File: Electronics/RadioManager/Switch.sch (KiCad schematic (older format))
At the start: 2 parts

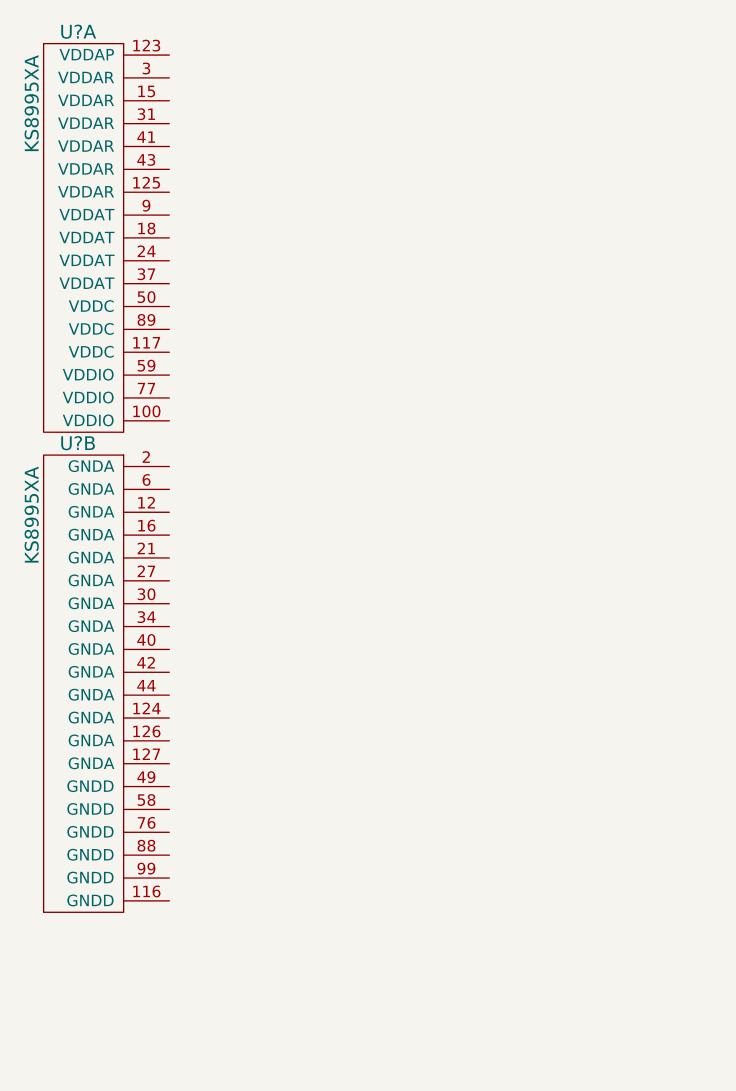
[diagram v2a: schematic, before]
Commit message: Replace switch with industrial version
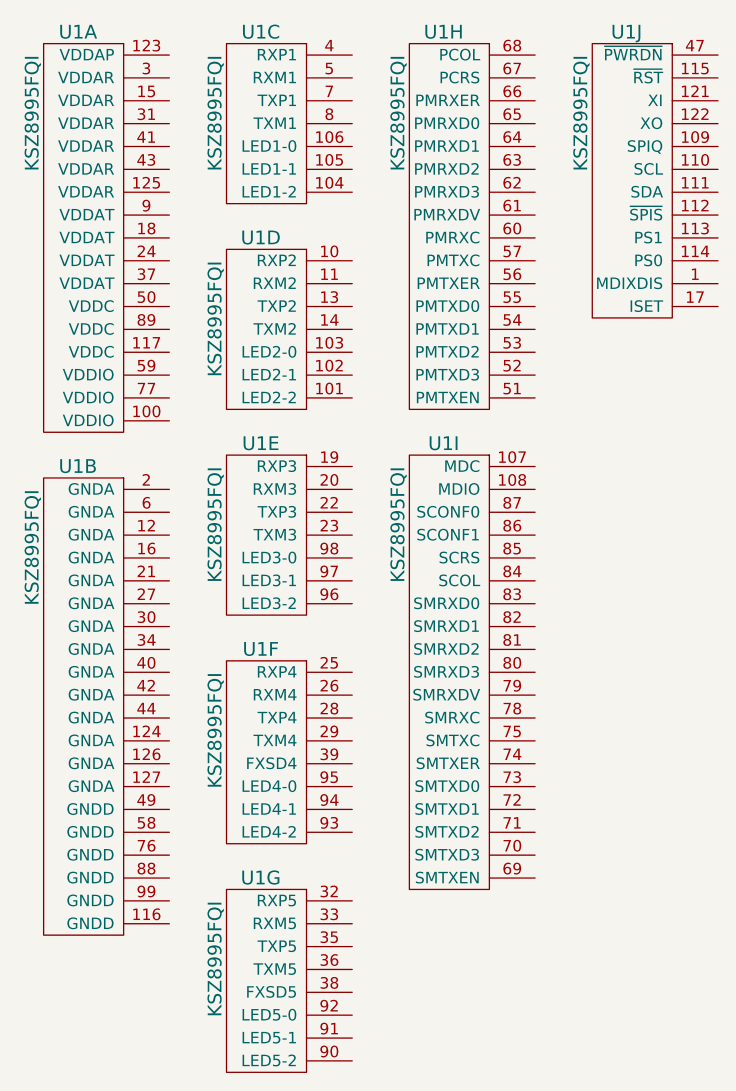
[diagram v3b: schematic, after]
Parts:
- removed U?: KS8995XA, ~, symbol KS8995XA
- added unit 2 of U1
- added unit 3 of U1
- added unit 4 of U1
- added unit 5 of U1
- added unit 6 of U1
- added unit 7 of U1
- added unit 8 of U1
- added unit 9 of U1
- added unit 10 of U1
- U1: renamed from U?; value KS8995XA -> KSZ8995FQI; Distributor Part No (none) -> 576-3300-ND; MFR Name (none) -> Micrel; MFR Part No (none) -> KSZ8995FQI
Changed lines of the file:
@@
 $EndDescr
 $Comp
-L KS8995XA U?
+L KS8995XA U1
 U 1 1 53DFFDCD
 P 1800 1700
-F 0 "U?" H 1800 1800 60  0000 C CNN
-F 1 "KS8995XA" V 1600 1700 60  0000 R CNN
+F 0 "U1" H 1800 1800 60  0000 C CNN
+F 1 "KSZ8995FQI" V 1600 1700 60  0000 R CNN
 F 2 "~" H 1800 1700 60  0000 C CNN
 F 3 "~" H 1800 1700 60  0000 C CNN
+F 4 "Micrel" H 1800 1700 60  0001 C CNN "MFR Name"
+F 5 "KSZ8995FQI" H 1800 1700 60  0001 C CNN "MFR Part No"
+F 6 "576-3300-ND" H 1800 1700 60  0001 C CNN "Distributor Part No"
 	1    1800 1700
 	1    0    0    -1
 $EndComp
 $Comp
-L KS8995XA U?
-U 2 1 53DFFDDC
-P 1800 3500
-F 0 "U?" H 1800 3600 60  0000 C CNN
-F 1 "KS8995XA" V 1600 3500 60  0000 R CNN
-F 2 "~" H 1800 3500 60  0000 C CNN
-F 3 "~" H 1800 3500 60  0000 C CNN
-	2    1800 3500
+L KS8995XA U1
+U 2 1 5410EF74
+P 1800 3600
+F 0 "U1" H 1800 3700 60  0000 C CNN
+F 1 "KSZ8995FQI" V 1600 3600 60  0000 R CNN
+F 2 "~" H 1800 3600 60  0000 C CNN
+F 3 "~" H 1800 3600 60  0000 C CNN
+F 4 "Micrel" H 1800 3600 60  0001 C CNN "MFR Name"
+F 5 "KSZ8995FQI" H 1800 3600 60  0001 C CNN "MFR Part No"
+F 6 "576-3300-ND" H 1800 3600 60  0001 C CNN "Distributor Part No"
+	2    1800 3600
 	1    0    0    -1
 $EndComp
+$Comp
+L KS8995XA U1
+U 3 1 5410EF88
+P 2600 1700
+F 0 "U1" H 2600 1800 60  0000 C CNN
+F 1 "KSZ8995FQI" V 2400 1700 60  0000 R CNN
+F 2 "~" H 2600 1700 60  0000 C CNN
+F 3 "~" H 2600 1700 60  0000 C CNN
+F 4 "Micrel" H 2600 1700 60  0001 C CNN "MFR Name"
+F 5 "KSZ8995FQI" H 2600 1700 60  0001 C CNN "MFR Part No"
+F 6 "576-3300-ND" H 2600 1700 60  0001 C CNN "Distributor Part No"
+	3    2600 1700
+	1    0    0    -1
+$EndComp
+$Comp
+L KS8995XA U1
+U 4 1 5410EF99
+P 2600 2600
+F 0 "U1" H 2600 2700 60  0000 C CNN
+F 1 "KSZ8995FQI" V 2400 2600 60  0000 R CNN
+F 2 "~" H 2600 2600 60  0000 C CNN
+F 3 "~" H 2600 2600 60  0000 C CNN
+F 4 "Micrel" H 2600 2600 60  0001 C CNN "MFR Name"
+F 5 "KSZ8995FQI" H 2600 2600 60  0001 C CNN "MFR Part No"
+F 6 "576-3300-ND" H 2600 2600 60  0001 C CNN "Distributor Part No"
+	4    2600 2600
+	1    0    0    -1
+$EndComp
+$Comp
+L KS8995XA U1
+U 5 1 5410EFAA
+P 2600 3500
+F 0 "U1" H 2600 3600 60  0000 C CNN
+F 1 "KSZ8995FQI" V 2400 3500 60  0000 R CNN
+F 2 "~" H 2600 3500 60  0000 C CNN
+F 3 "~" H 2600 3500 60  0000 C CNN
+F 4 "Micrel" H 2600 3500 60  0001 C CNN "MFR Name"
+F 5 "KSZ8995FQI" H 2600 3500 60  0001 C CNN "MFR Part No"
+F 6 "576-3300-ND" H 2600 3500 60  0001 C CNN "Distributor Part No"
+	5    2600 3500
+	1    0    0    -1
+$EndComp
+$Comp
+L KS8995XA U1
+U 6 1 5410EFBB
+P 2600 4400
+F 0 "U1" H 2600 4500 60  0000 C CNN
+F 1 "KSZ8995FQI" V 2400 4400 60  0000 R CNN
+F 2 "~" H 2600 4400 60  0000 C CNN
+F 3 "~" H 2600 4400 60  0000 C CNN
+F 4 "Micrel" H 2600 4400 60  0001 C CNN "MFR Name"
+F 5 "KSZ8995FQI" H 2600 4400 60  0001 C CNN "MFR Part No"
+F 6 "576-3300-ND" H 2600 4400 60  0001 C CNN "Distributor Part No"
+	6    2600 4400
+	1    0    0    -1
+$EndComp
+$Comp
+L KS8995XA U1
+U 7 1 5410EFCC
+P 2600 5400
+F 0 "U1" H 2600 5500 60  0000 C CNN
+F 1 "KSZ8995FQI" V 2400 5400 60  0000 R CNN
+F 2 "~" H 2600 5400 60  0000 C CNN
+F 3 "~" H 2600 5400 60  0000 C CNN
+F 4 "Micrel" H 2600 5400 60  0001 C CNN "MFR Name"
+F 5 "KSZ8995FQI" H 2600 5400 60  0001 C CNN "MFR Part No"
+F 6 "576-3300-ND" H 2600 5400 60  0001 C CNN "Distributor Part No"
+	7    2600 5400
+	1    0    0    -1
+$EndComp
+$Comp
+L KS8995XA U1
+U 8 1 5410EFDD
+P 3400 1700
+F 0 "U1" H 3400 1800 60  0000 C CNN
+F 1 "KSZ8995FQI" V 3200 1700 60  0000 R CNN
+F 2 "~" H 3400 1700 60  0000 C CNN
+F 3 "~" H 3400 1700 60  0000 C CNN
+F 4 "Micrel" H 3400 1700 60  0001 C CNN "MFR Name"
+F 5 "KSZ8995FQI" H 3400 1700 60  0001 C CNN "MFR Part No"
+F 6 "576-3300-ND" H 3400 1700 60  0001 C CNN "Distributor Part No"
+	8    3400 1700
+	1    0    0    -1
+$EndComp
+$Comp
+L KS8995XA U1
+U 9 1 5410EFEE
+P 3400 3500
+F 0 "U1" H 3400 3600 60  0000 C CNN
+F 1 "KSZ8995FQI" V 3200 3500 60  0000 R CNN
+F 2 "~" H 3400 3500 60  0000 C CNN
+F 3 "~" H 3400 3500 60  0000 C CNN
+F 4 "Micrel" H 3400 3500 60  0001 C CNN "MFR Name"
+F 5 "KSZ8995FQI" H 3400 3500 60  0001 C CNN "MFR Part No"
+F 6 "576-3300-ND" H 3400 3500 60  0001 C CNN "Distributor Part No"
+	9    3400 3500
+	1    0    0    -1
+$EndComp
+$Comp
+L KS8995XA U1
+U 10 1 5410EFFF
+P 4200 1700
+F 0 "U1" H 4200 1800 60  0000 C CNN
+F 1 "KSZ8995FQI" V 4000 1700 60  0000 R CNN
+F 2 "~" H 4200 1700 60  0000 C CNN
+F 3 "~" H 4200 1700 60  0000 C CNN
+F 4 "Micrel" H 4200 1700 60  0001 C CNN "MFR Name"
+F 5 "KSZ8995FQI" H 4200 1700 60  0001 C CNN "MFR Part No"
+F 6 "576-3300-ND" H 4200 1700 60  0001 C CNN "Distributor Part No"
+	10   4200 1700
+	1    0    0    -1
+$EndComp

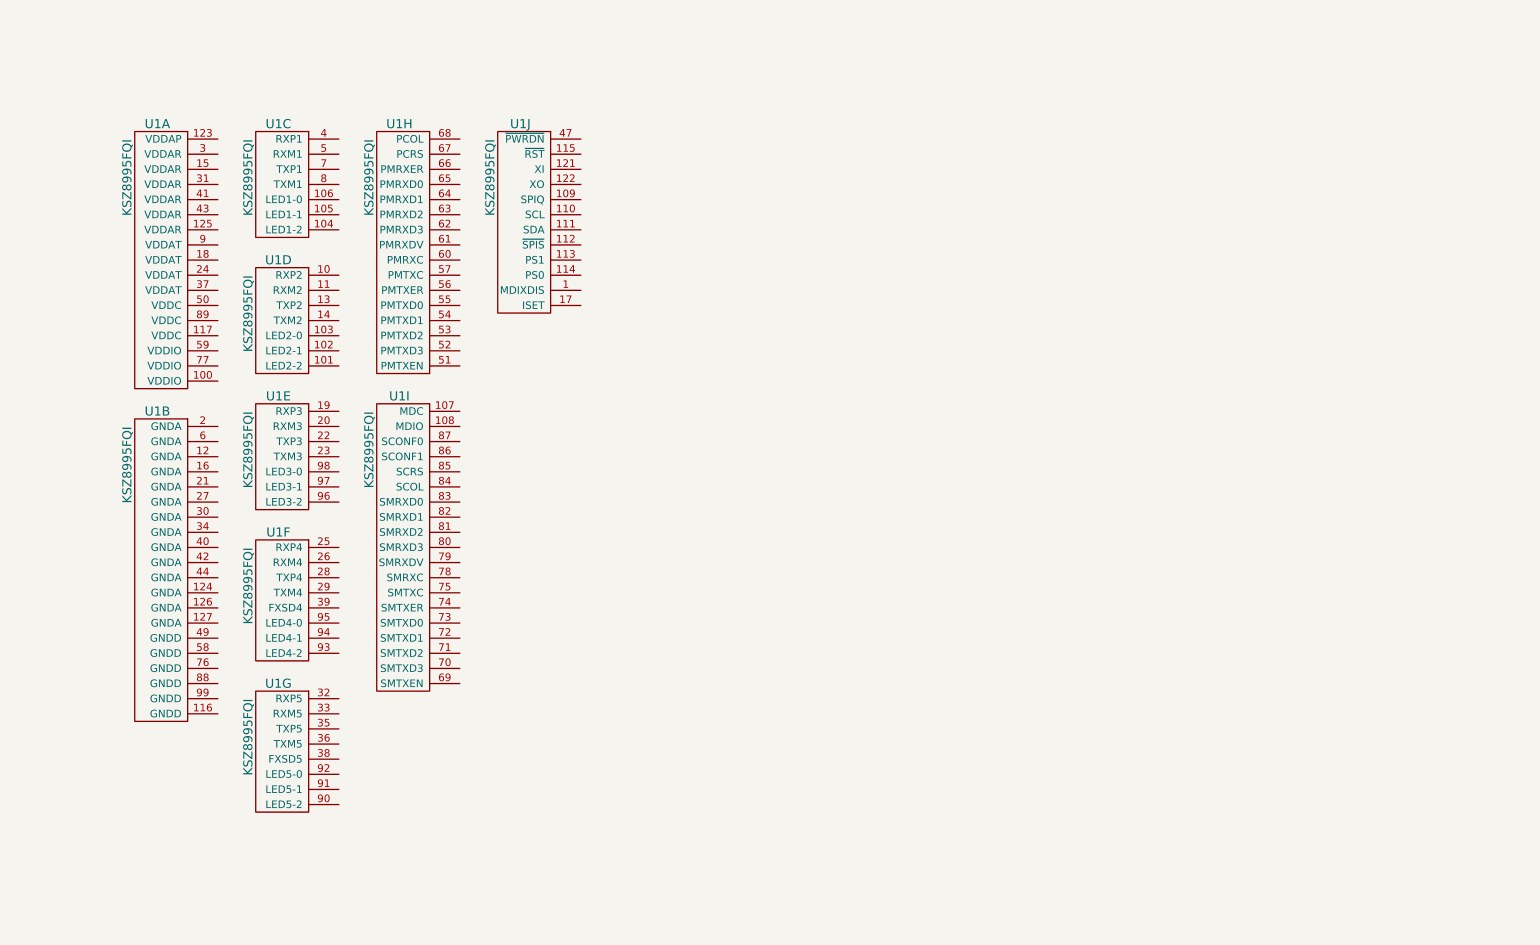
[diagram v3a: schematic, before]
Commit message: Switch power connections
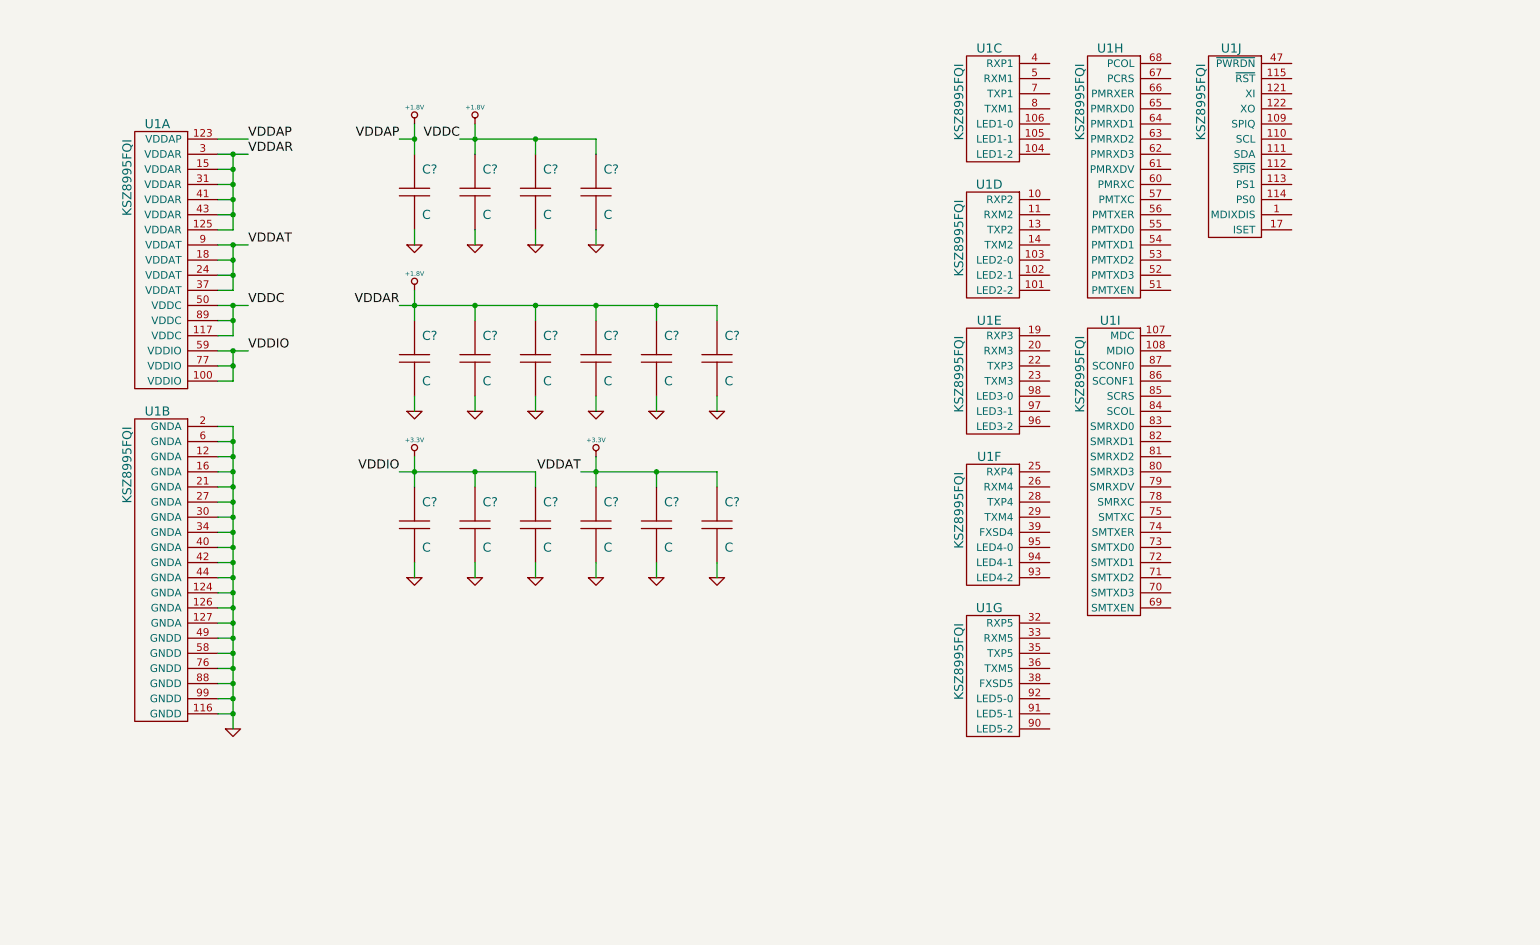
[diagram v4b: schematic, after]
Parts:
- added C? (x16): C, ~, symbol C
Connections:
- net +3.3V: now reaches U1.100 (VDDIO)
- net +3.3V: now also U1.18 (VDDAT), U1.24 (VDDAT), U1.37 (VDDAT), U1.59 (VDDIO), U1.77 (VDDIO), U1.9 (VDDAT), C?.1, C?.1, C?.1, C?.1, C?.1, C?.1
- net +1.8V: now reaches U1.117 (VDDC)
- net +1.8V: now also U1.123 (VDDAP), U1.125 (VDDAR), U1.15 (VDDAR), U1.3 (VDDAR), U1.31 (VDDAR), U1.41 (VDDAR), U1.43 (VDDAR), U1.50 (VDDC), U1.89 (VDDC), C?.1, C?.1, C?.1, C?.1, C?.1, C?.1, C?.1, C?.1, C?.1, C?.1
- net GND: now reaches U1.116 (GNDD)
- net GND: now also U1.12 (GNDA), U1.124 (GNDA), U1.126 (GNDA), U1.127 (GNDA), U1.16 (GNDA), U1.2 (GNDA), U1.21 (GNDA), U1.27 (GNDA), U1.30 (GNDA), U1.34 (GNDA), U1.40 (GNDA), U1.42 (GNDA), U1.44 (GNDA), U1.49 (GNDD), U1.58 (GNDD), U1.6 (GNDA), U1.76 (GNDD), U1.88 (GNDD), U1.99 (GNDD), C?.2, C?.2, C?.2, C?.2, C?.2, C?.2, C?.2, C?.2, C?.2, C?.2, C?.2, C?.2, C?.2, C?.2, C?.2, C?.2
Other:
- moved on the sheet: U1C, U1D, U1E, U1F, U1G, U1H, U1I, U1J

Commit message: Add port connections
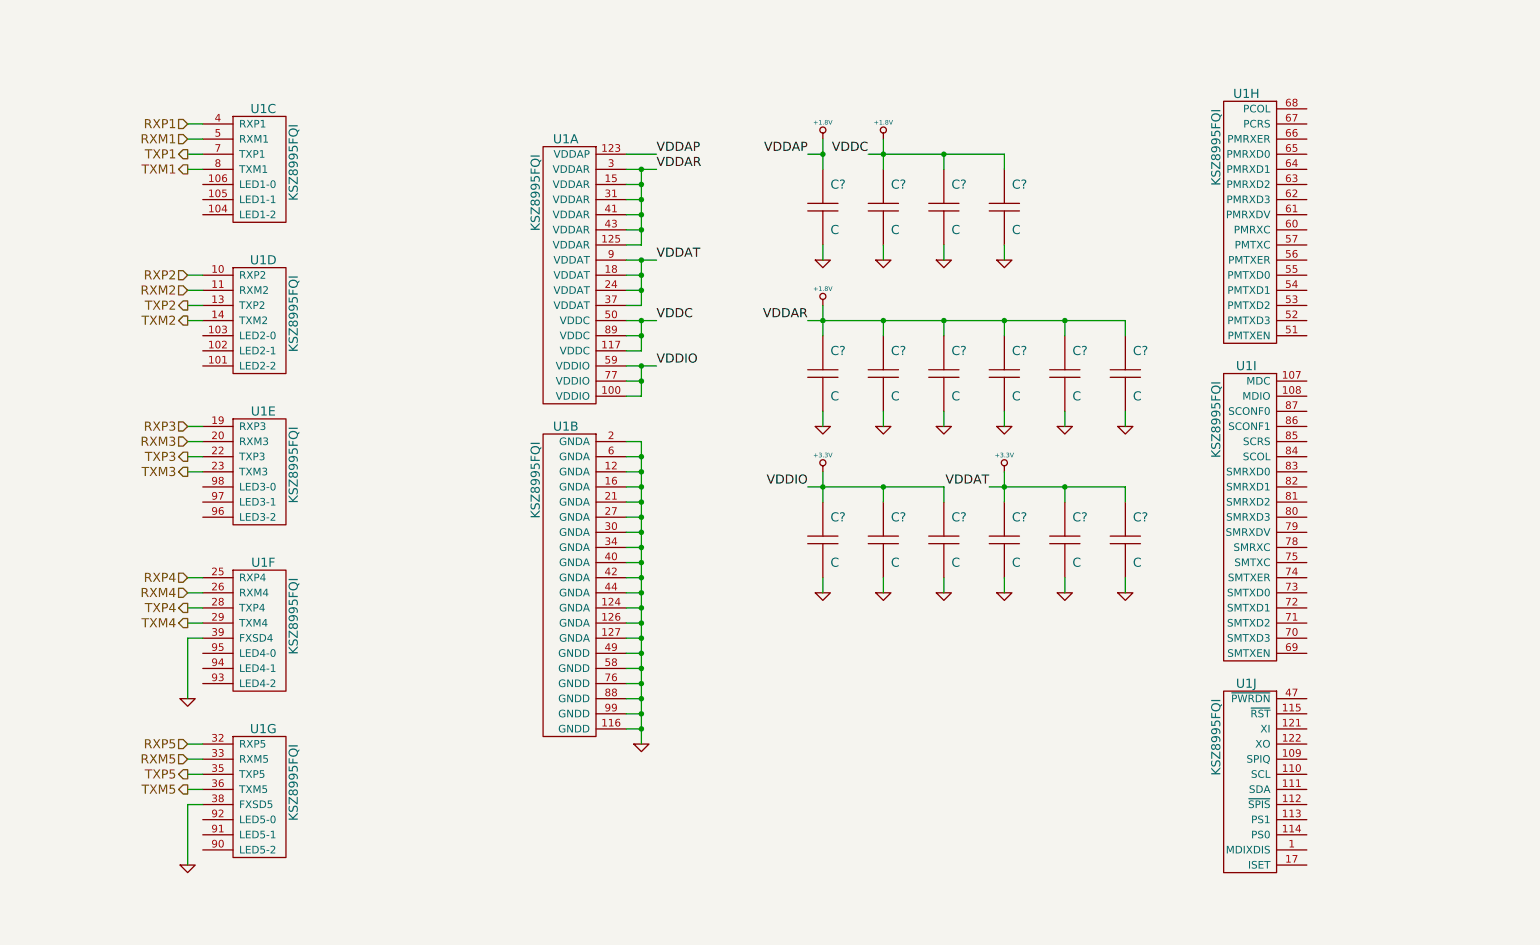
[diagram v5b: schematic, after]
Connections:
- net GND: now also U1.38 (FXSD5), U1.39 (FXSD4)
- net RXP1: now reaches U1.4 (RXP1)
- net RXM1: now reaches U1.5 (RXM1)
- net TXP1: now reaches U1.7 (TXP1)
- net TXM1: now reaches U1.8 (TXM1)
- net RXP2: now reaches U1.10 (RXP2)
- net RXM2: now reaches U1.11 (RXM2)
- net TXP2: now reaches U1.13 (TXP2)
- net TXM2: now reaches U1.14 (TXM2)
- net RXP3: now reaches U1.19 (RXP3)
- net RXM3: now reaches U1.20 (RXM3)
- net TXP3: now reaches U1.22 (TXP3)
- net TXM3: now reaches U1.23 (TXM3)
- net RXP4: now reaches U1.25 (RXP4)
- net RXM4: now reaches U1.26 (RXM4)
- net TXP4: now reaches U1.28 (TXP4)
- net TXM4: now reaches U1.29 (TXM4)
- net RXP5: now reaches U1.32 (RXP5)
- net RXM5: now reaches U1.33 (RXM5)
- net TXP5: now reaches U1.35 (TXP5)
- net TXM5: now reaches U1.36 (TXM5)
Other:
- moved on the sheet: C?, U1A, U1B, U1C, U1D, U1E, U1F, U1G, U1H, U1I, U1J
